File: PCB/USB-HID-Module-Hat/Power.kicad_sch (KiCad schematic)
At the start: 12 parts, among them J3 1757242, M1 D24V22F5, M2 D24V22F3

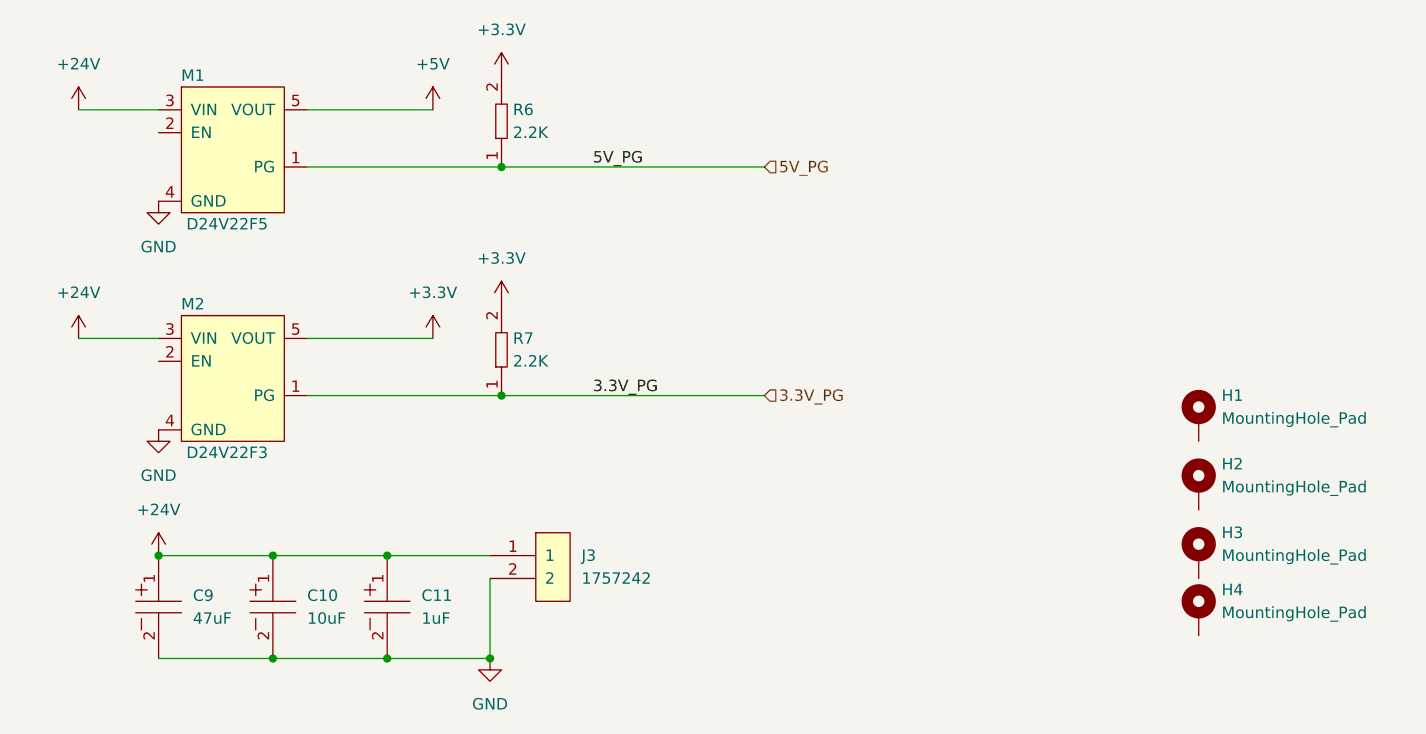
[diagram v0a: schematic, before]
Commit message: PCB
PCB layout 80% complete. Board shape defined. Components and connectors places !
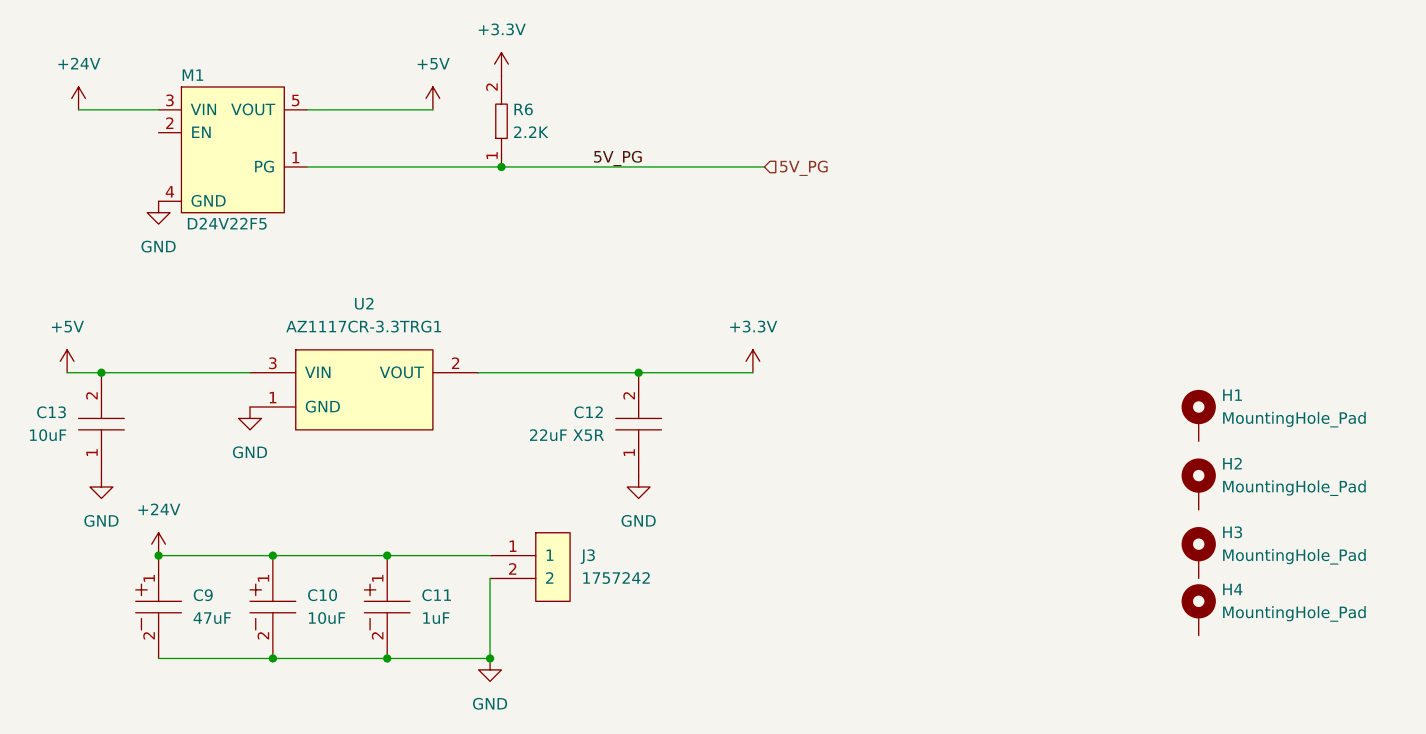
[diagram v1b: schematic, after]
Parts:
- removed M2: D24V22F3, AVR-KiCAD-Lib-Modules:D24V22F12, symbol AVR-KiCAD-Lib-Modules:D24V22F3
- removed R7: RC0603FR-072K2L, AVR-KiCAD-Lib-Resistors:R0603, symbol AVR-KiCAD-Lib-Resistors:RC0603FR-072K2L
- added C12: GRM21BR61A226ME51L, AVR-KiCAD-Lib-Capacitors:C0805, symbol AVR-KiCAD-Lib-Capacitors:GRM21BR61A226ME51L
- added C13: GRT31CR61H106KE01L, AVR-KiCAD-Lib-Capacitors:C1206, symbol AVR-KiCAD-Lib-Capacitors:GRT31CR61H106KE01L
- added U2: AZ1117CR-3.3TRG1, AVR-KiCAD-Lib-ICs:SOT_89, symbol AVR-KiCAD-Lib-ICs:AZ1117CR-3.3TRG1
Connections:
- net +3.3V: now also C12.2, U2.2 (VOUT)
- net +5V: now also C13.2, U2.3 (VIN)
- net GND: now also C12.1, C13.1, U2.1 (GND)
